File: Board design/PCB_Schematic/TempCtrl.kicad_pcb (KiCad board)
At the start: 4 copper layers, 80 x 100 mm, 190 parts, among them CON1 BARREL_JACK, IC1 ATMEGA328P-A, J1 5V_Outputs_1, J2 External ref, J3 5V_Outputs_2, P1 233-2977, P2 820-8104, P3 RS485, P4 USB_OTG, P5 ICSP, P6 ADC breakout, SW1 DISABLE_COMMS, U1 LM7805, U10 INA330, U11 ISO7242, U12 FT232RL, U13 ADS1262, U14 AD8639, U15 DAC8564, U16 AD8639, U17 DAC8564, U18 74LS125, U2 TMA0505S, U3 ADuM7642CRQZ, U4 ISO3088, U5 OPA548, U6 OPA548, U7 OPA548, U8 OPA548, U9 INA330, X1 TSX-3225 X1E0000210013

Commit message: Expand courtyard of connector
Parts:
- P5: footprint Pin_Headers:Pin_Header_Straight_2x03 -> Custom:6pin_3x2_Amphenol_75869-131LF

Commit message: Version bump and compile
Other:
- board text added: "Temperature Controller V5.3 - Charles Baynham 2020"
- board text removed: "Temperature Controller V5.2 - Charles Baynham 2020"
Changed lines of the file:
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@@
     (effects (font (size 1 1) (thickness 0.25)) (justify left))
   )
-  (gr_text "Temperature Controller V5.2 - Charles Baynham 2020" (at 173 133) (layer F.Cu)
+  (gr_text "Temperature Controller V5.3 - Charles Baynham 2020" (at 173 133) (layer F.Cu)
     (effects (font (size 1.5 1.5) (thickness 0.3) italic) (justify left))
   )

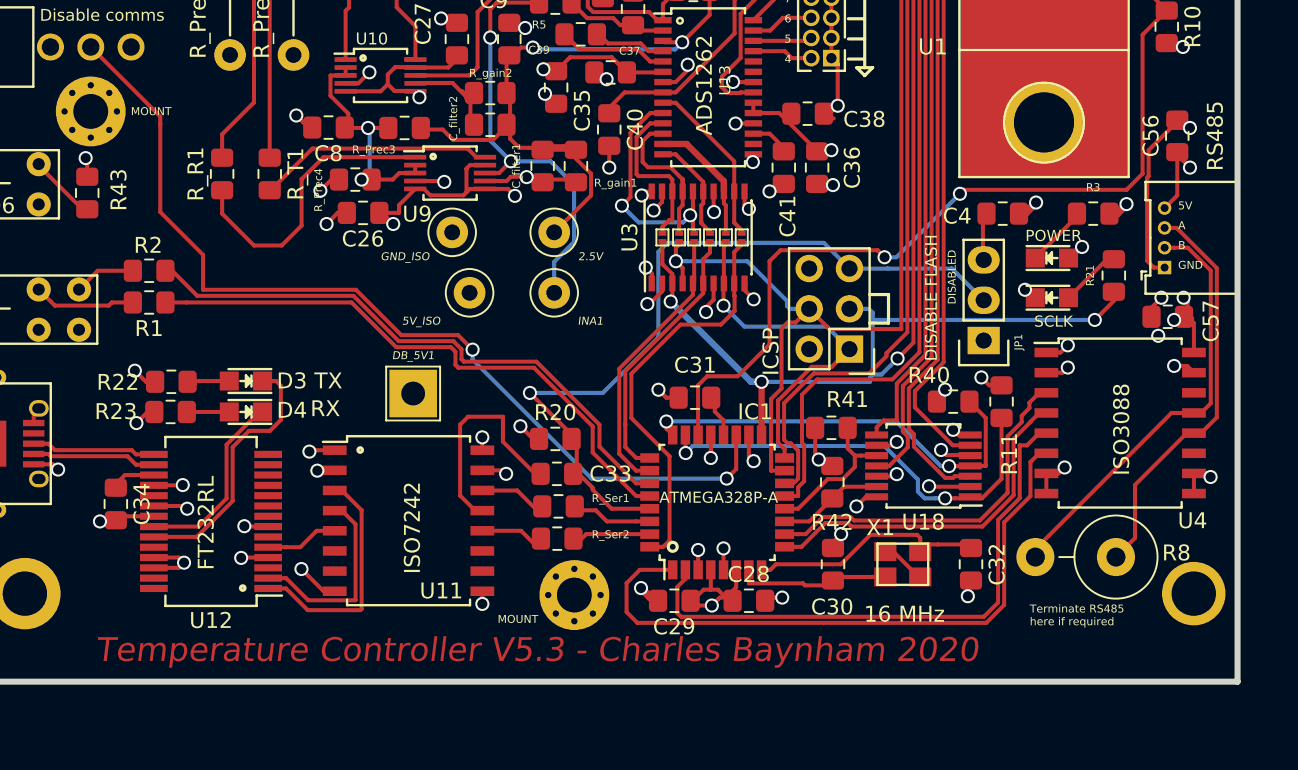
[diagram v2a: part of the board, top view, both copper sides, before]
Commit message: Move resistors slightly to avoid ISCP connector
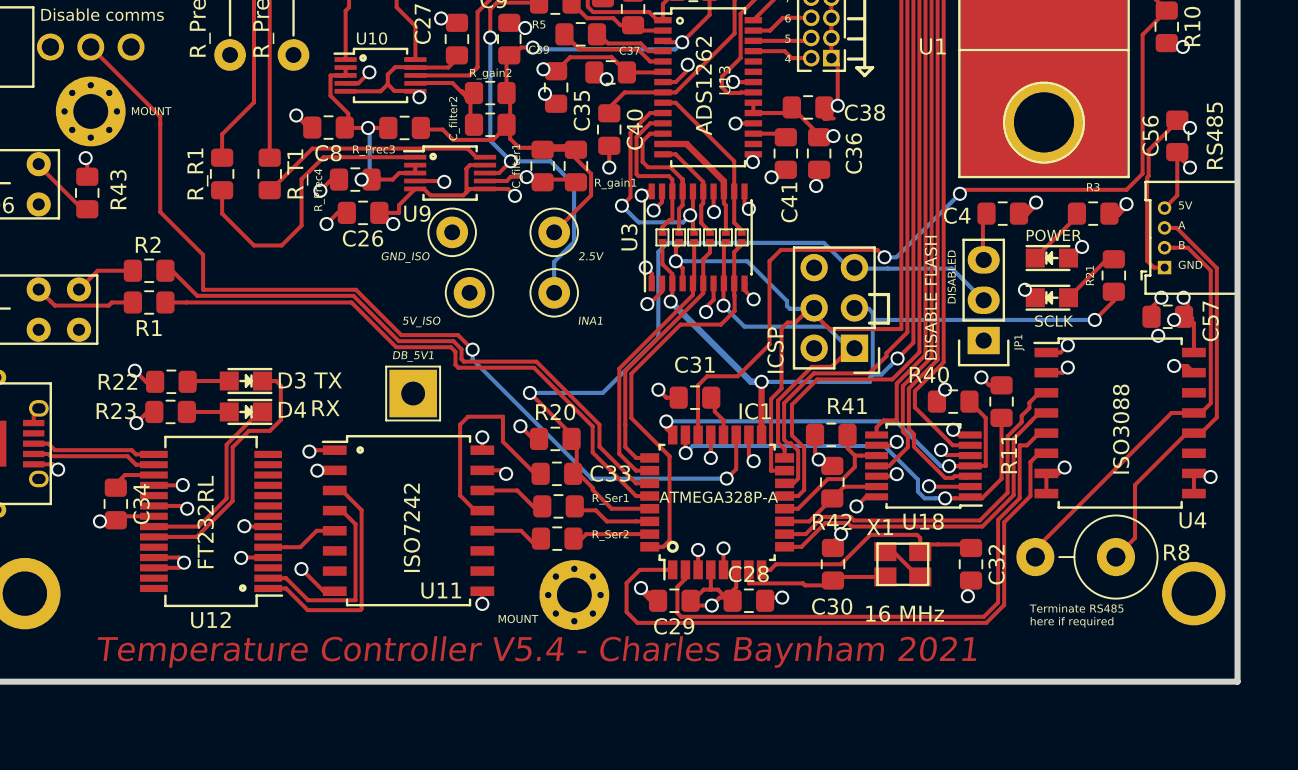
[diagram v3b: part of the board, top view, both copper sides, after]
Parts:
- moved C36 0.90 mm to (218.6, 101.7)
- moved C41 0.90 mm to (216.5, 101.7)
- moved R41 0.44 mm to (219.4, 119.4)
- moved C38 0.40 mm to (217.9, 98.8)
- moved P5 0.32 mm to (220.9, 114.0)
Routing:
- net /ANALOG_GND: track 40.5 -> 41.0 mm
- net /DAC_CS2: track 72.3 -> 72.8 mm
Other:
- board text added: "Temperature Controller V5.4 - Charles Baynham 2021"
- board text removed: "Temperature Controller V5.3 - Charles Baynham 2020"

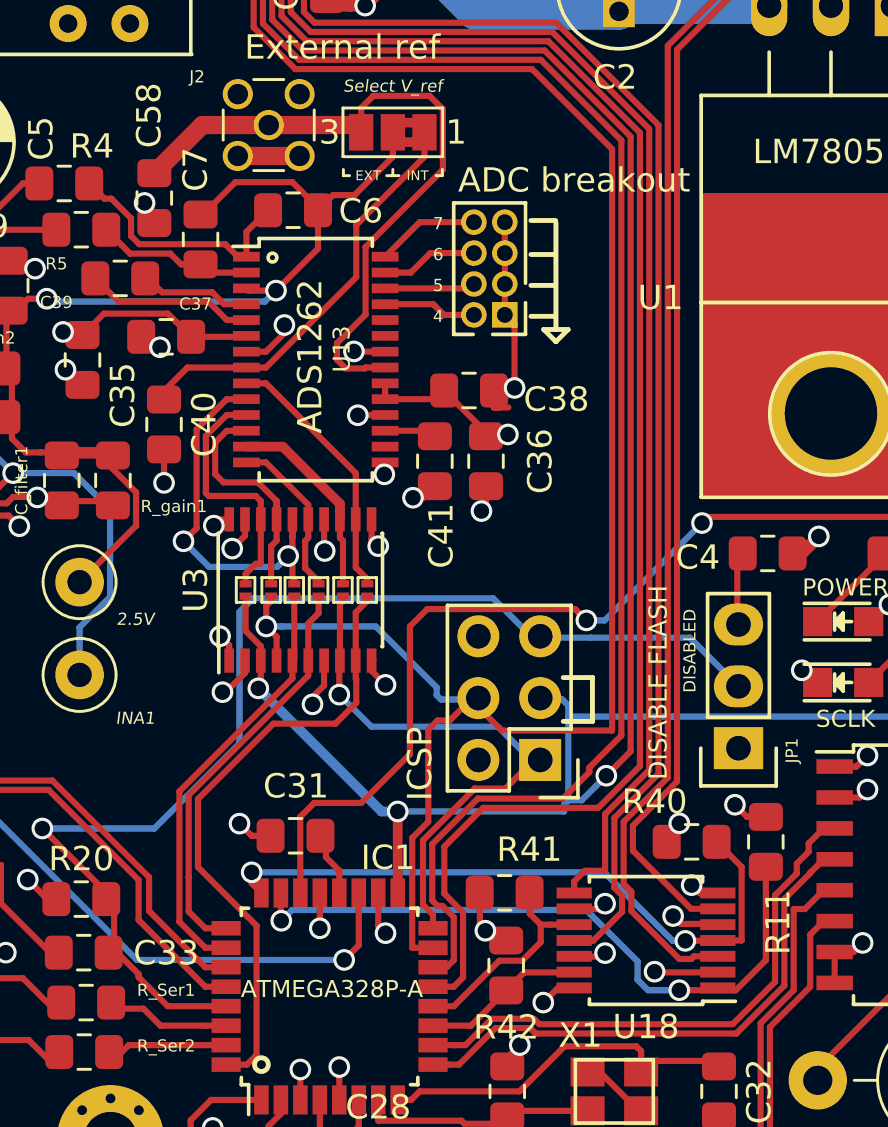
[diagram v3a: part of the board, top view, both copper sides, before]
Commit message: Move isolator too: that connector is massive
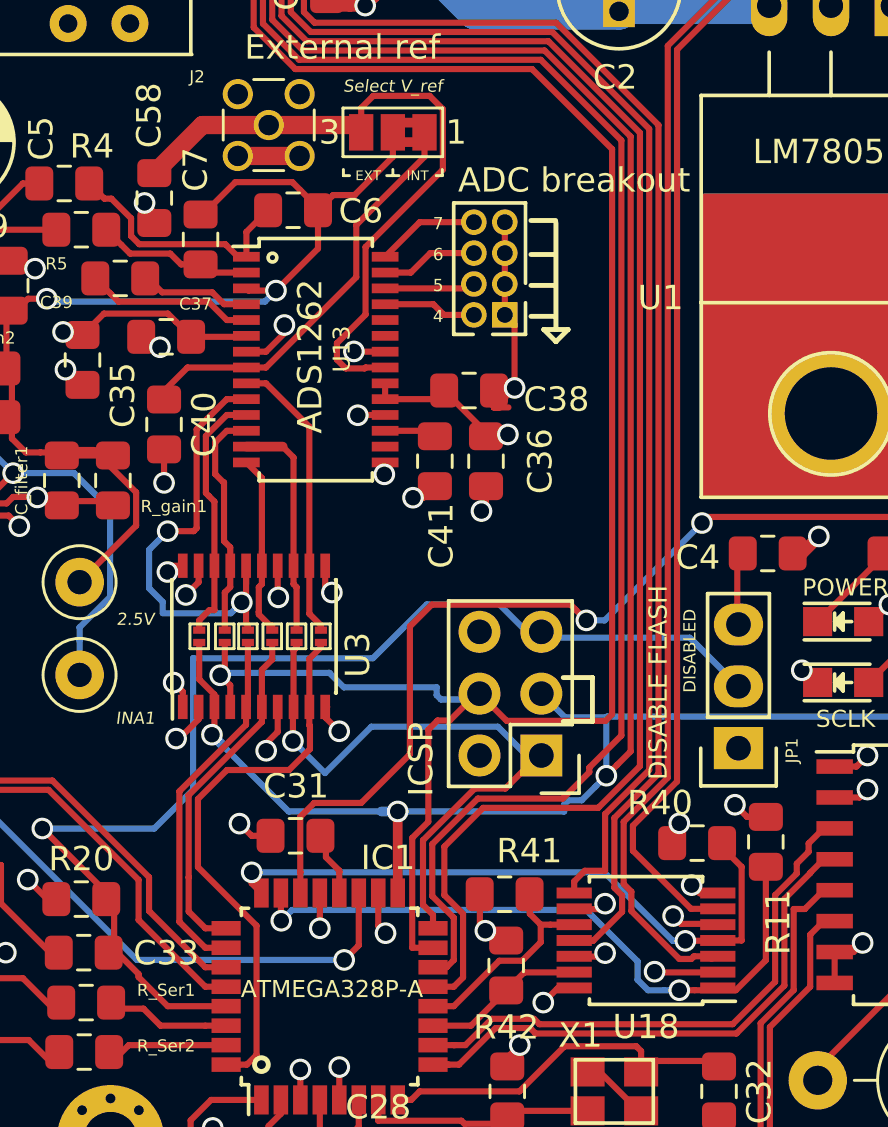
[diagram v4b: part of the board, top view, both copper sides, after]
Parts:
- moved JP2 2.69 mm to (206.8, 108.9)
- moved JP3 2.69 mm to (207.9, 108.9)
- moved JP4 2.69 mm to (211.8, 108.9)
- moved JP5 2.69 mm to (209.8, 108.9)
- moved JP6 2.69 mm to (210.8, 108.9)
- moved JP7 2.69 mm to (208.8, 108.9)
- moved U3 2.69 mm to (209.1, 108.9)
- moved R40 0.23 mm to (227.3, 117.4)
- moved P5 0.19 mm to (220.9, 113.8)
- moved R41 0.06 mm to (219.4, 119.5)
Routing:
- net /ADC_CS_ISO: track 15.9 -> 18.8 mm
- net /ADC_DRDY: track 17.0 -> 14.3 mm
- net /ADC_CS: track 17.7 -> 15.0 mm
- net /MISO: track 22.8 -> 25.5 mm
- net /ADC_START: track 26.2 -> 23.5 mm
- net /ADC_DRDY_ISO: track 7.24 -> 8.48 mm
- net /MISO_ISO: track 8.15 -> 9.27 mm
- net /ADC_START_ISO: track 10.8 -> 11.9 mm
- net /SCLK: track 106.3 -> 105.6 mm

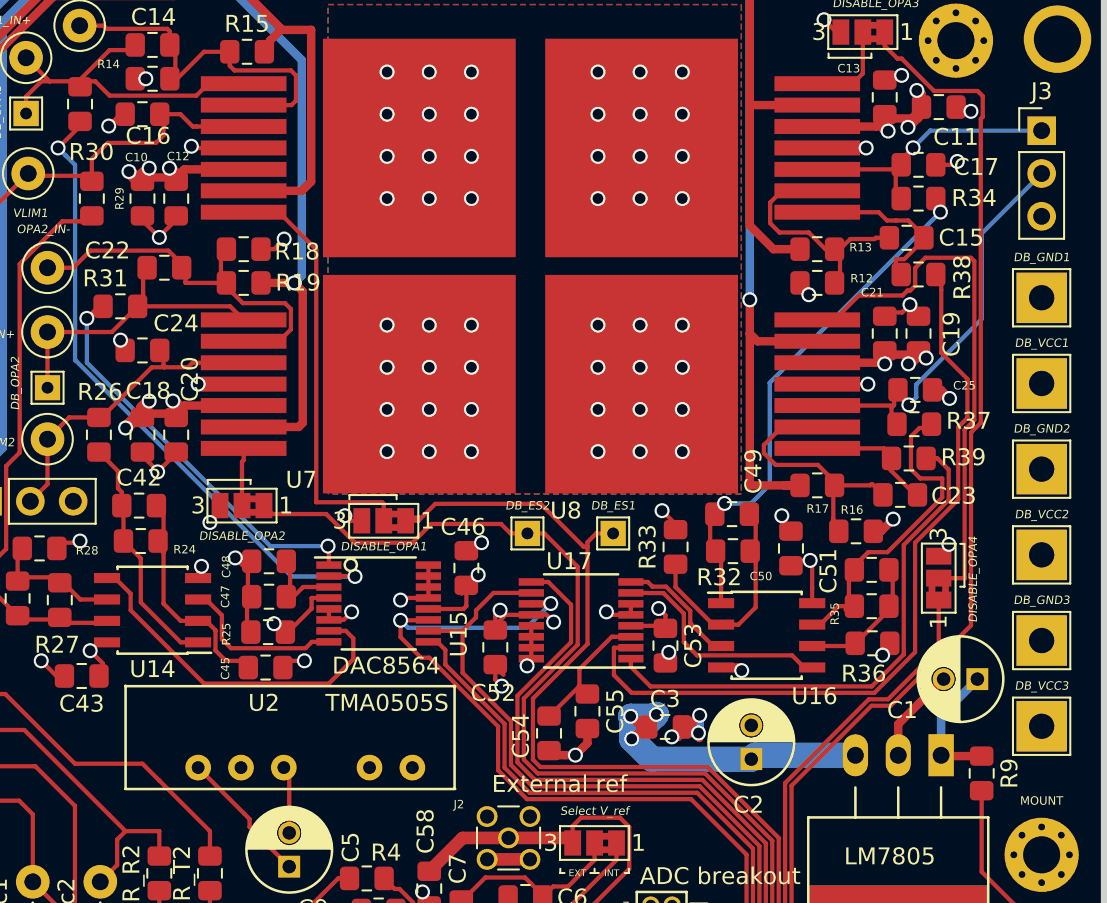
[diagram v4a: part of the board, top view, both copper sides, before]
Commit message: Remove VLIM capacitors - these were pushing opamps dangerously close to instability
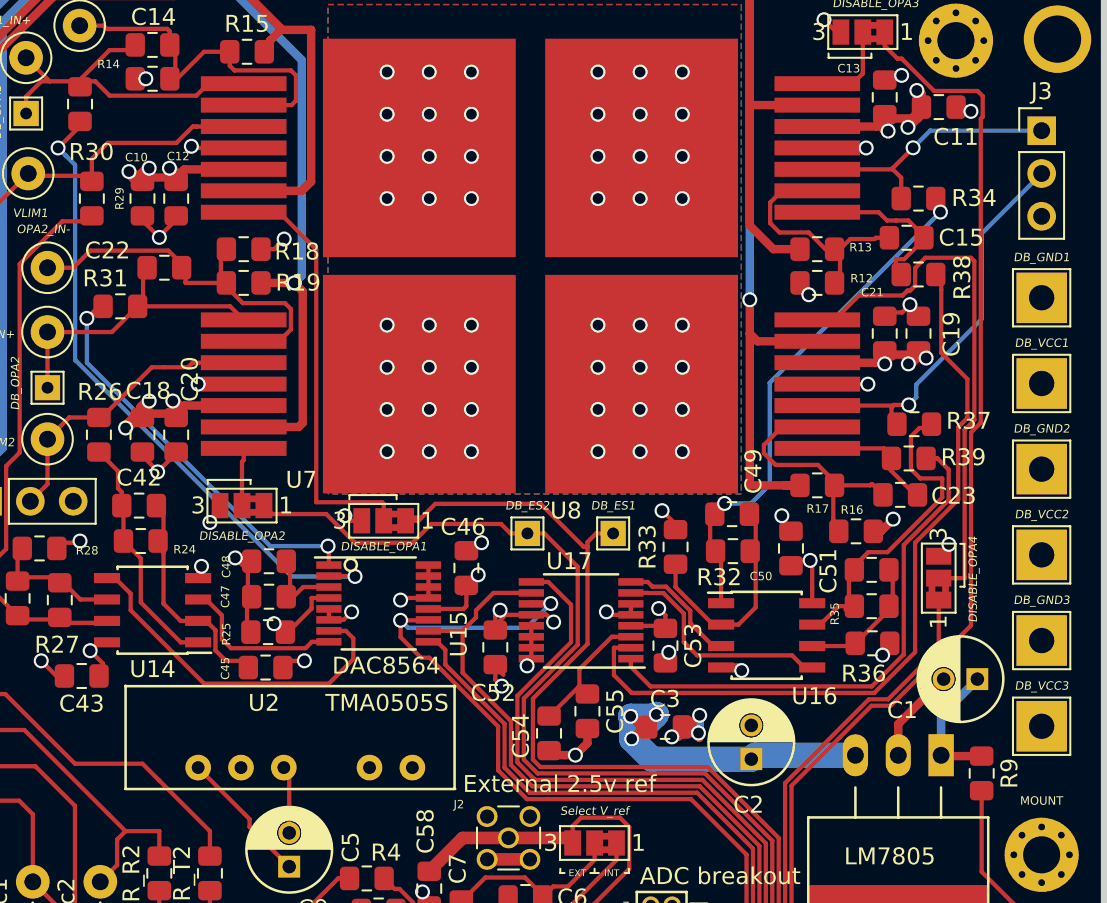
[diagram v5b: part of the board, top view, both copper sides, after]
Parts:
- removed C16, C17, C24, C25: 10n, Capacitor_SMD:C_0805_2012Metric_Pad1.15x1.40mm_HandSolder
- J2: value External ref -> External 2.5v ref
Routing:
- net Earth_Clean: track 119.5 -> 115.7 mm, vias 115 -> 111
- net /VLIM1: track 36.5 -> 35.2 mm
- net /VLIM4: track 24.7 -> 23.6 mm
- net /VLIM2: track 18.6 -> 17.6 mm

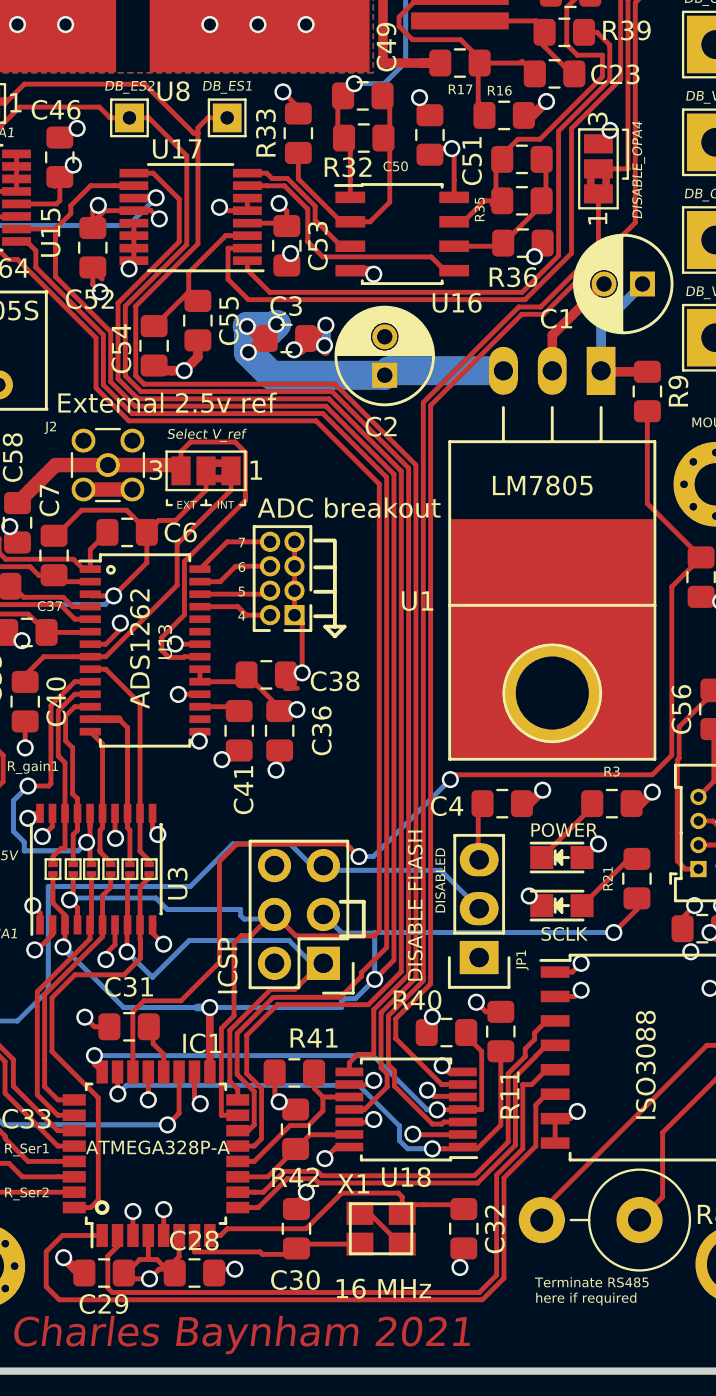
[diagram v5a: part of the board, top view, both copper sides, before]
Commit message: Expand footprint of U18
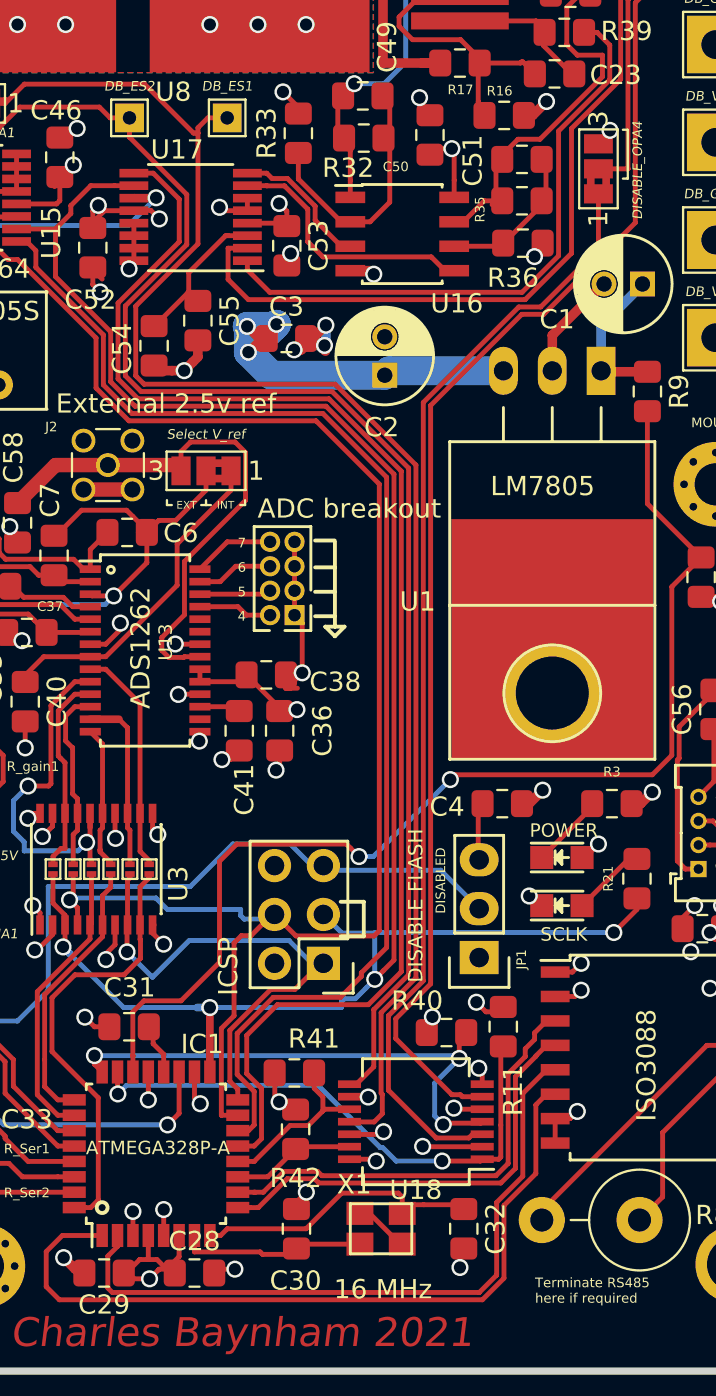
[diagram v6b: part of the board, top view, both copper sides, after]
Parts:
- U18: footprint Package_SO:TSSOP-14_4.4x5mm_P0.65mm -> Package_SO:SSOP-14_5.3x6.2mm_P0.65mm
- moved U18 0.81 mm to (225.7, 122.0)
- moved R11 0.28 mm to (230.3, 117.1)
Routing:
- net /ES3_OUT: track 91.7 -> 92.9 mm
- net /ES2_OUT: track 84.1 -> 83.1 mm
- net /ES4_IN: track 27.4 -> 28.5 mm
- net /ES4_OUT: track 56.3 -> 57.3 mm
- net /ES3_IN: track 26.6 -> 27.6 mm, vias 2 -> 3
- net /RS485_RE: track 22.9 -> 23.6 mm
- net /RS485_R: track 23.0 -> 23.6 mm
- net Earth_Clean: track 115.7 -> 115.2 mm
